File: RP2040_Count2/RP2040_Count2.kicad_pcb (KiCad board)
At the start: 2 copper layers, 59 x 29.5 mm, 18 parts, among them J2 String1, J3 OLED, SW1 Test, U1 74AHCT1G125, U2 rp2040-zero, U3 AMS1117-5.0, U4 INA219BxD

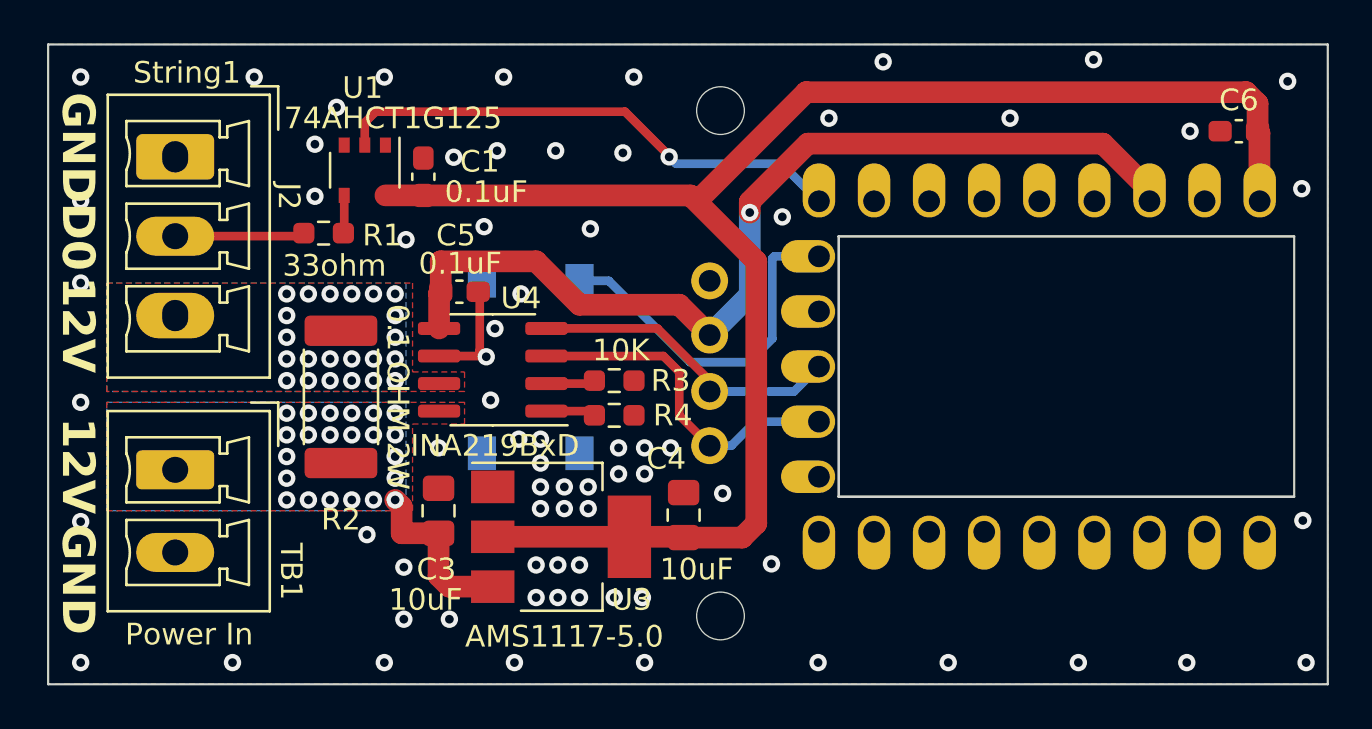
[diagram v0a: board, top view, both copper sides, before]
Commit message: add plug in 3 to 4 adapter
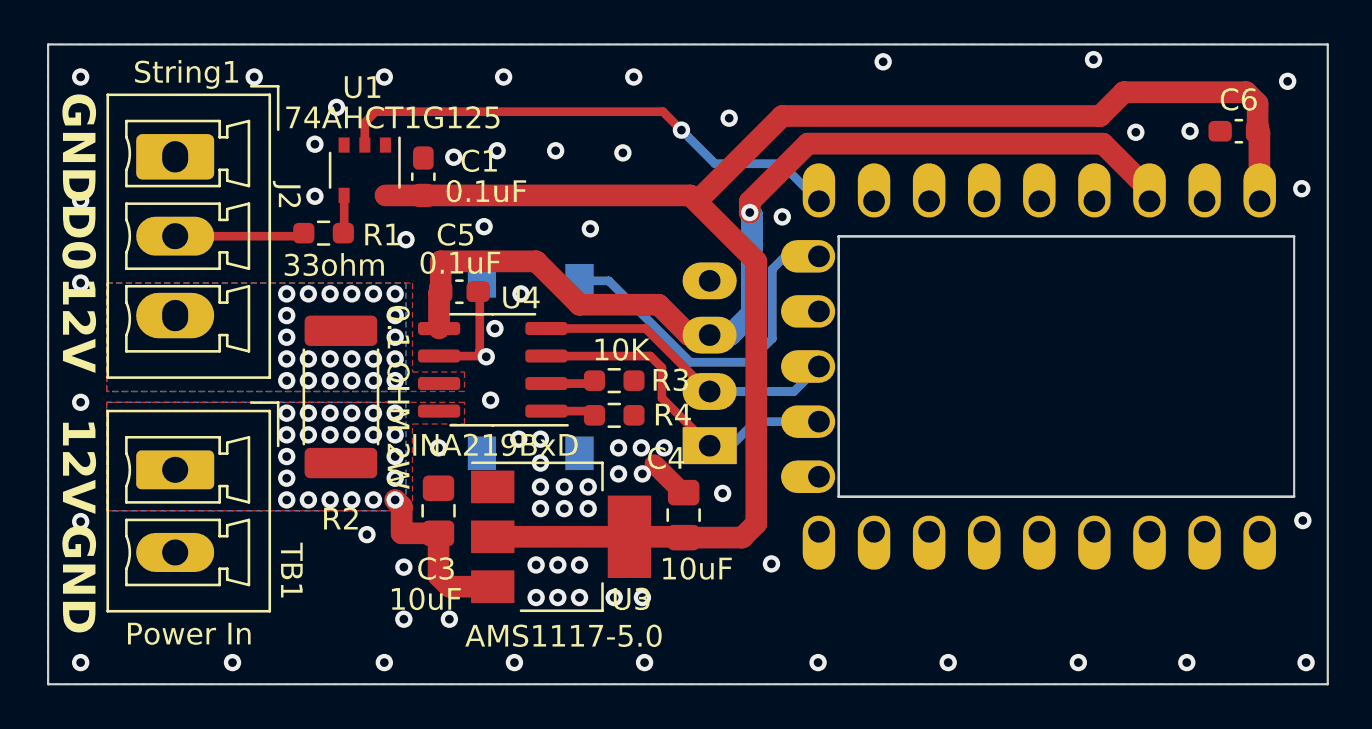
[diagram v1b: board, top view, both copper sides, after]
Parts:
- J3: footprint Scotts:OLED-SSD1306-128X64-I2C-THT_2HOLE -> Scotts:OLED-SSD1306-128X64-I2C-THT_SCOTT2
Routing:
- net GND: track 5.34 -> 7.87 mm
- net +3.3V: track 44.8 -> 45.4 mm
